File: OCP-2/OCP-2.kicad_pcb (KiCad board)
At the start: 2 copper layers, 90 x 100 mm, 176 parts, among them X1 ico*отверстие*М3, X2 ico*отверстие*М3, X3 ico*отверстие*М3, X4 ico*отверстие*М3

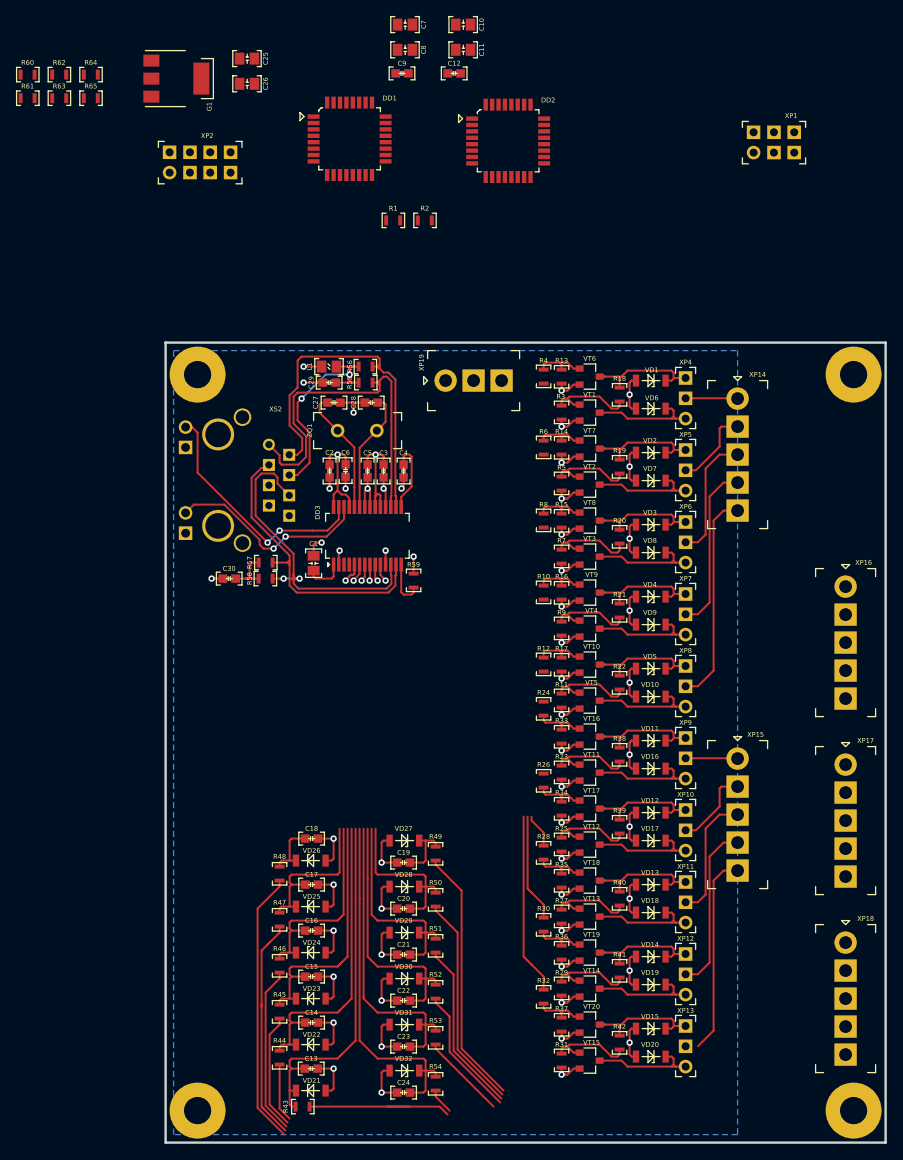
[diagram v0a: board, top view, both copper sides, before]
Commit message: перенесены клеммники, +LDO, +прог.разъем, +МК расположение
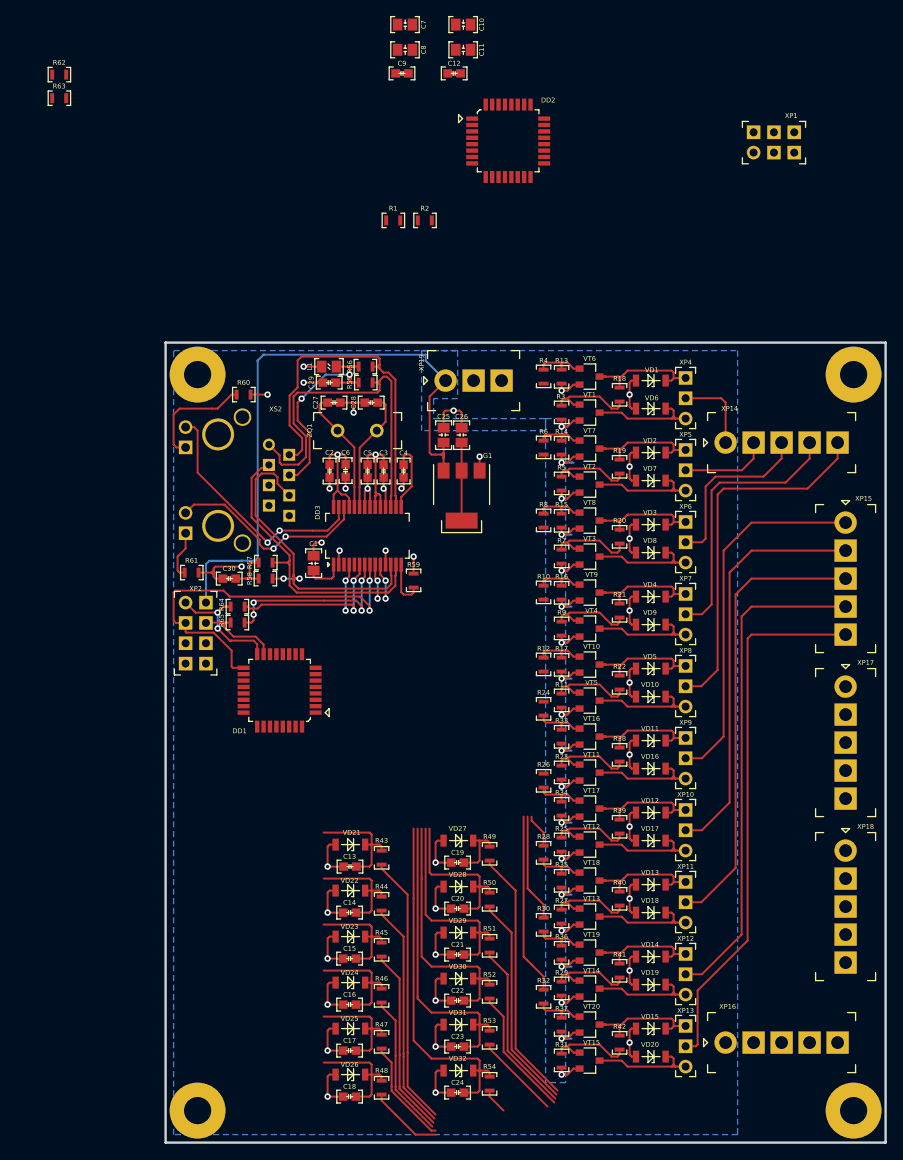
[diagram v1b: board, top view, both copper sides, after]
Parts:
- moved DD1 74.5 mm to (68.5, 96.2), turned to 180 degrees
- moved R64 69.0 mm to (59.0, 83.0), turned to 180 degrees
- moved R65 68.1 mm to (59.0, 85.0), turned to 180 degrees
- moved G1 63.2 mm to (87.0, 69.2), turned to 270 degrees
- moved R61 62.7 mm to (53.2, 78.8)
- moved XP16 58.9 mm to (120.0, 137.5), turned to 0 degrees
- moved C25 54.4 mm to (84.8, 62.5), turned to 90 degrees
- moved XP2 53.8 mm to (52.5, 82.5), turned to 270 degrees
- moved C26 52.7 mm to (87.0, 62.5), turned to 90 degrees
- moved R60 48.3 mm to (59.8, 56.5)
- moved R43 32.7 mm to (77.0, 114.4), turned to 270 degrees
- moved C18 32.6 mm to (73.0, 144.2), turned to 0 degrees
- moved XP15 32.4 mm to (135.0, 72.5)
- moved VD21 30.8 mm to (71.2, 112.8), turned to 0 degrees
- moved R48 29.6 mm to (77.0, 143.1)
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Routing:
- net 5V: track 39.4 -> 117.4 mm
- net /ETH.CLK: track 2.02 -> 48.3 mm, vias 1 -> 2
- net /DOUT10: track 25.0 -> 67.4 mm
- net /DOUT7: track 10.1 -> 51.3 mm
- net /DOUT9: track 21.1 -> 62.3 mm
- net /DOUT8: track 15.9 -> 56.8 mm
- net /DOUT6: track 6.46 -> 45.8 mm
- net /MC.DIN1: track 44.8 -> 14.5 mm
- net GND: track 180.4 -> 209.1 mm, vias 44 -> 47
- net /DIN6: track 34.3 -> 9.26 mm
- net /MC.DIN2: track 38.1 -> 14.5 mm
- net Net-(DD3-Pad7): track 2.17 -> 23.8 mm, vias 1 -> 4
- net /DIN2: track 7.27 -> 28.7 mm
- net /DOUT5: track 26.6 -> 45.6 mm
- net Net-(DD3-Pad6): track 2.31 -> 20.6 mm, vias 1 -> 2
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- added copper zone on B.Cu, net 5V

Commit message: завершенеа трассировка
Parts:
- removed C11, C8: Конденсатор*10мкФ*16В*0805, N_RLC:Конденсатор_SMD_IEC_0805
- added C31: Конденсатор*10мкФ*16В*0805, N_RLC:Конденсатор_SMD_IEC_0805, F.Cu at (85.5, 76.0)
- added X5: ico*LOGO_NIKITOS_10х10, N_ICO:ni_10x10, F.Cu at (72.8, 115.0)
- moved C10 99.5 mm to (83.2, 109.8), turned to 270 degrees
- moved R62 89.3 mm to (54.8, 104.0)
- moved R63 84.5 mm to (54.8, 102.0)
- moved DD2 83.2 mm to (80.0, 104.8), turned to 90 degrees
- moved C7 82.9 mm to (73.8, 93.0)
- moved C9 77.0 mm to (58.5, 90.5), turned to 90 degrees
- moved C12 75.9 mm to (84.8, 92.2), turned to 90 degrees
- moved XP1 72.0 mm to (90.0, 90.0), turned to 270 degrees
- moved R1 64.2 mm to (56.8, 95.1), turned to 270 degrees
- moved R2 57.7 mm to (86.8, 92.2), turned to 90 degrees
- moved C19 38.0 mm to (60.2, 142.5)
- moved R49 38.0 mm to (64.2, 141.4)
- moved VD27 38.0 mm to (58.5, 139.8)
- moved C24 23.5 mm to (72.0, 125.2)
- moved R54 23.5 mm to (76.0, 124.1)
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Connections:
- C13 pad 2: /MC.DIN1 -> /MC.DIN7
- C14 pad 2: /MC.DIN2 -> /MC.DIN6
- C15 pad 2: /MC.DIN3 -> /MC.DIN5
- C16 pad 2: /MC.DIN4 -> /MC.DIN1
- C17 pad 2: /MC.DIN5 -> /MC.DIN2
- C18 pad 2: /MC.DIN6 -> /MC.DIN3
- C19 pad 2: /MC.DIN7 -> /MC.DIN4
- C20 pad 2: /MC.DIN8 -> /MC.DIN12
- C21 pad 2: /MC.DIN9 -> /MC.DIN11
- C23 pad 2: /MC.DIN11 -> /MC.DIN9
- C24 pad 2: /MC.DIN12 -> /MC.DIN8
- DD1 pad 1: /MC.DIN1 -> /MC.DIN7
- DD1 pad 10: /MC.DIN4 -> /MC.OUT3
- DD1 pad 11: /MC.DIN5 -> /MC.OUT2
- DD1 pad 12: /MC.DIN6 -> /MC.OUT1
- DD1 pad 19: Net-(DD1-Pad19) -> /MC.DIN4
- DD1 pad 2: /MC.DIN2 -> /MC.DIN8
- DD1 pad 22: Net-(DD1-Pad22) -> /MC.DIN3
- DD1 pad 23: /MC.OUT1 -> /MC.DIN2
- DD1 pad 24: /MC.OUT2 -> /MC.DIN1
- DD1 pad 25: /MC.OUT3 -> /MC.DIN5
- DD1 pad 26: /MC.OUT4 -> /MC.DIN6
- DD1 pad 7: Net-(DD1-Pad7) -> /MC.OUT6
- DD1 pad 8: Net-(DD1-Pad8) -> /MC.OUT5
- DD1 pad 9: /MC.DIN3 -> /MC.OUT4
- DD2 pad 1: Net-(DD2-Pad1) -> /MC.DIN12
- DD2 pad 10: /MC.DIN8 -> Net-(DD2-Pad10)
- DD2 pad 11: /MC.DIN9 -> /MC.OUT10
- DD2 pad 12: /MC.DIN10 -> /MC.OUT9
- DD2 pad 13: /MC.DIN11 -> /MC.OUT8
- DD2 pad 14: /MC.DIN12 -> /MC.OUT7
- DD2 pad 23: /MC.OUT5 -> Net-(DD2-Pad23)
- DD2 pad 24: /MC.OUT6 -> Net-(DD2-Pad24)
- DD2 pad 25: /MC.OUT7 -> Net-(DD2-Pad25)
- DD2 pad 26: /MC.OUT8 -> Net-(DD2-Pad26)
- DD2 pad 30: /MC.OUT9 -> /MC.DIN9
- DD2 pad 31: /MC.OUT10 -> /MC.DIN10
- DD2 pad 32: Net-(DD2-Pad32) -> /MC.DIN11
- DD2 pad 9: /MC.DIN7 -> Net-(DD2-Pad9)
- R43 pad 1: /MC.DIN1 -> /MC.DIN7
- R43 pad 2: /DIN1 -> /DIN7
- R44 pad 1: /MC.DIN2 -> /MC.DIN6
- R44 pad 2: /DIN2 -> /DIN6
- R45 pad 1: /MC.DIN3 -> /MC.DIN5
- R45 pad 2: /DIN3 -> /DIN5
- R46 pad 1: /MC.DIN4 -> /MC.DIN1
- R46 pad 2: /DIN4 -> /DIN1
- R47 pad 1: /MC.DIN5 -> /MC.DIN2
- R47 pad 2: /DIN5 -> /DIN2
- R48 pad 1: /MC.DIN6 -> /MC.DIN3
- R48 pad 2: /DIN6 -> /DIN3
- R49 pad 1: /MC.DIN7 -> /MC.DIN4
- R49 pad 2: /DIN7 -> /DIN4
- R50 pad 1: /MC.DIN8 -> /MC.DIN12
- R50 pad 2: /DIN8 -> /DIN12
- R51 pad 1: /MC.DIN9 -> /MC.DIN11
- R51 pad 2: /DIN9 -> /DIN11
- R53 pad 1: /MC.DIN11 -> /MC.DIN9
- R53 pad 2: /DIN11 -> /DIN9
- R54 pad 1: /MC.DIN12 -> /MC.DIN8
- R54 pad 2: /DIN12 -> /DIN8
- VD21 pad 2: /MC.DIN1 -> /MC.DIN7
- VD22 pad 2: /MC.DIN2 -> /MC.DIN6
- VD23 pad 2: /MC.DIN3 -> /MC.DIN5
- VD24 pad 2: /MC.DIN4 -> /MC.DIN1
- VD25 pad 2: /MC.DIN5 -> /MC.DIN2
- VD26 pad 2: /MC.DIN6 -> /MC.DIN3
- VD27 pad 2: /MC.DIN7 -> /MC.DIN4
- VD28 pad 2: /MC.DIN8 -> /MC.DIN12
- VD29 pad 2: /MC.DIN9 -> /MC.DIN11
- VD31 pad 2: /MC.DIN11 -> /MC.DIN9
- VD32 pad 2: /MC.DIN12 -> /MC.DIN8
- XP16 pad 1: /DIN1 -> /DIN4
- XP16 pad 2: /DIN2 -> /DIN3
- XP16 pad 3: /DIN3 -> /DIN2
- XP16 pad 4: /DIN4 -> /DIN1
- XP17 pad 1: /DIN5 -> /DIN12
- XP17 pad 2: /DIN6 -> /DIN11
- XP17 pad 3: /DIN7 -> /DIN10
- XP17 pad 4: /DIN8 -> /DIN9
- XP18 pad 1: /DIN9 -> /DIN8
- XP18 pad 2: /DIN10 -> /DIN7
- XP18 pad 3: /DIN11 -> /DIN6
- XP18 pad 4: /DIN12 -> /DIN5
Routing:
- net 3V3: track 49.7 -> 232.3 mm, vias 3 -> 11
- net /DIN12: track 3.22 -> 99.5 mm
- net /DIN11: track 10.8 -> 92.0 mm
- net /DIN6: track 9.26 -> 82.4 mm
- net /DIN8: track 27.0 -> 97.3 mm
- net /DIN10: track 16.4 -> 84.4 mm
- net /DIN4: track 18.1 -> 80.7 mm
- net /DIN5: track 13.4 -> 75.8 mm
- net /MC.OUT1: track 0.00 -> 61.4 mm
- net /DIN3: track 23.4 -> 81.6 mm
- net GND: track 209.1 -> 267.2 mm, vias 47 -> 70
- net /DIN7: track 32.3 -> 89.1 mm
- net /DIN2: track 28.7 -> 83.2 mm
- net /DIN9: track 21.7 -> 76.1 mm
- net /MC.OUT2: track 0.00 -> 53.4 mm
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- added copper zone on B.Cu, net 3V3
- added copper zone on F.Cu, net GND
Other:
- board text added: "1+"
- board text added: "1-"
- board text added: "10+"
- board text added: "10-"
- board text added: "10C"
- board text added: "1C"
- board text added: "2+"
- board text added: "2-"
- board text added: "2C"
- board text added: "3+"
- board text added: "3-"
- board text added: "3C"
- board text added: "4+"
- board text added: "4-"
- board text added: "4C"
- board text added: "5+"
- board text added: "5-"
- board text added: "5C"
- board text added: "5V"
- board text added: "6+"
- board text added: "6-"
- board text added: "6C"
- board text added: "7+"
- board text added: "7-"
- board text added: "7C"
- board text added: "8+"
- board text added: "8-"
- board text added: "8C"
- board text added: "9+"
- board text added: "9-"
- board text added: "9C"
- board text added: "GND"
- board text added: "M.IN1"
- board text added: "M.IN2"
- board text added: "M.IN3"
- board text added: "M.IN4"
- board text added: "M.IN5"
- board text added: "M.IN6"
- board text added: "M.IN7"
- board text added: "M.IN8"
- board text added: "M.IN9"
- board text added: "M.OUT1"
- board text added: "M.OUT2"
- board text added: "M.OUT3"
- board text added: "M.OUT4"
- board text added: "M.OUT5"
- board text added: "M.OUT6"
- board text added: "MASTER"
- board text added: "MI"
- board text added: "MO"
- board text added: "N.C."
- board text added: "RES"
- board text added: "RX"
- board text added: "S.IN10"
- board text added: "S.IN11"
- board text added: "S.IN12"
- board text added: "S.OUT10"
- board text added: "S.OUT7"
- board text added: "S.OUT8"
- board text added: "S.OUT9"
- board text added: "SCK"
- board text added: "SLAVE"
- board text added: "TX"

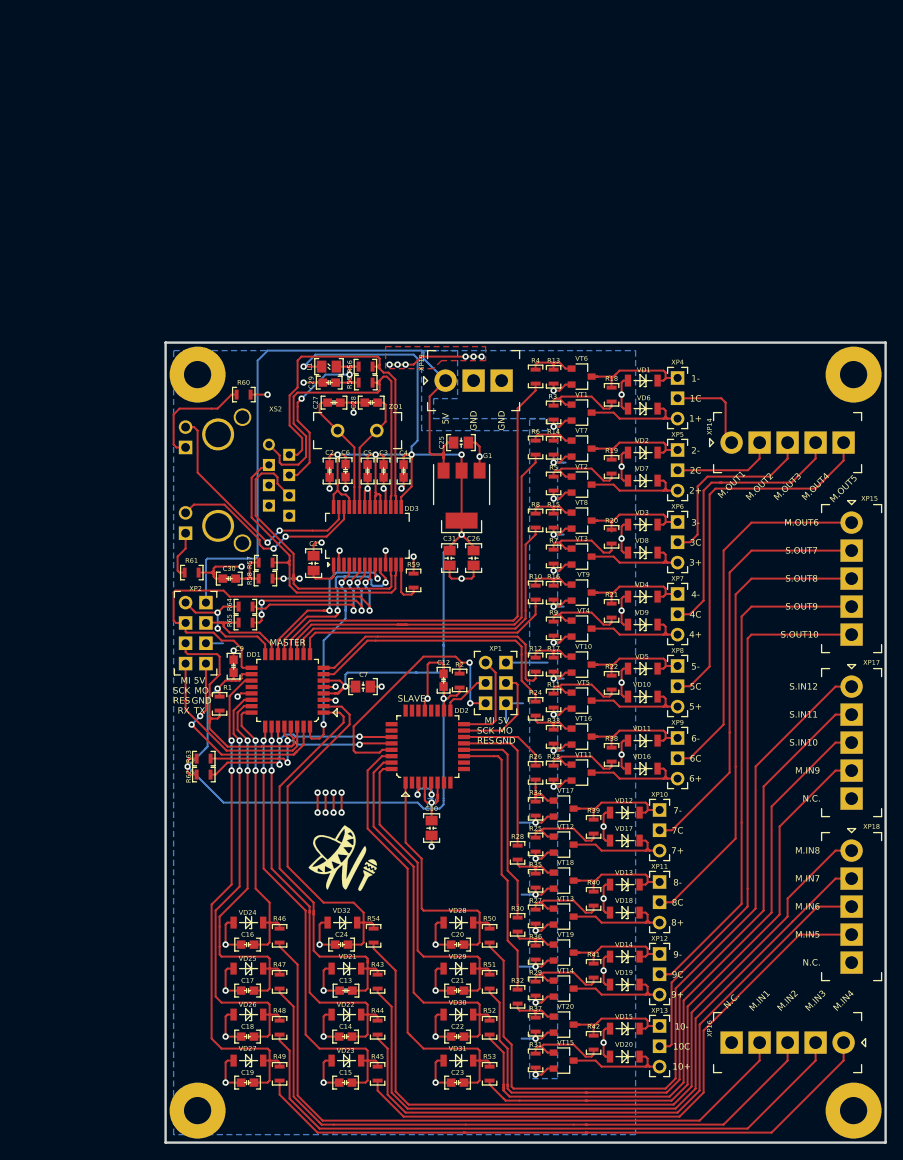
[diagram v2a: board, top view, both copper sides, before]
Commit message: добавлена поясняющая маркировка
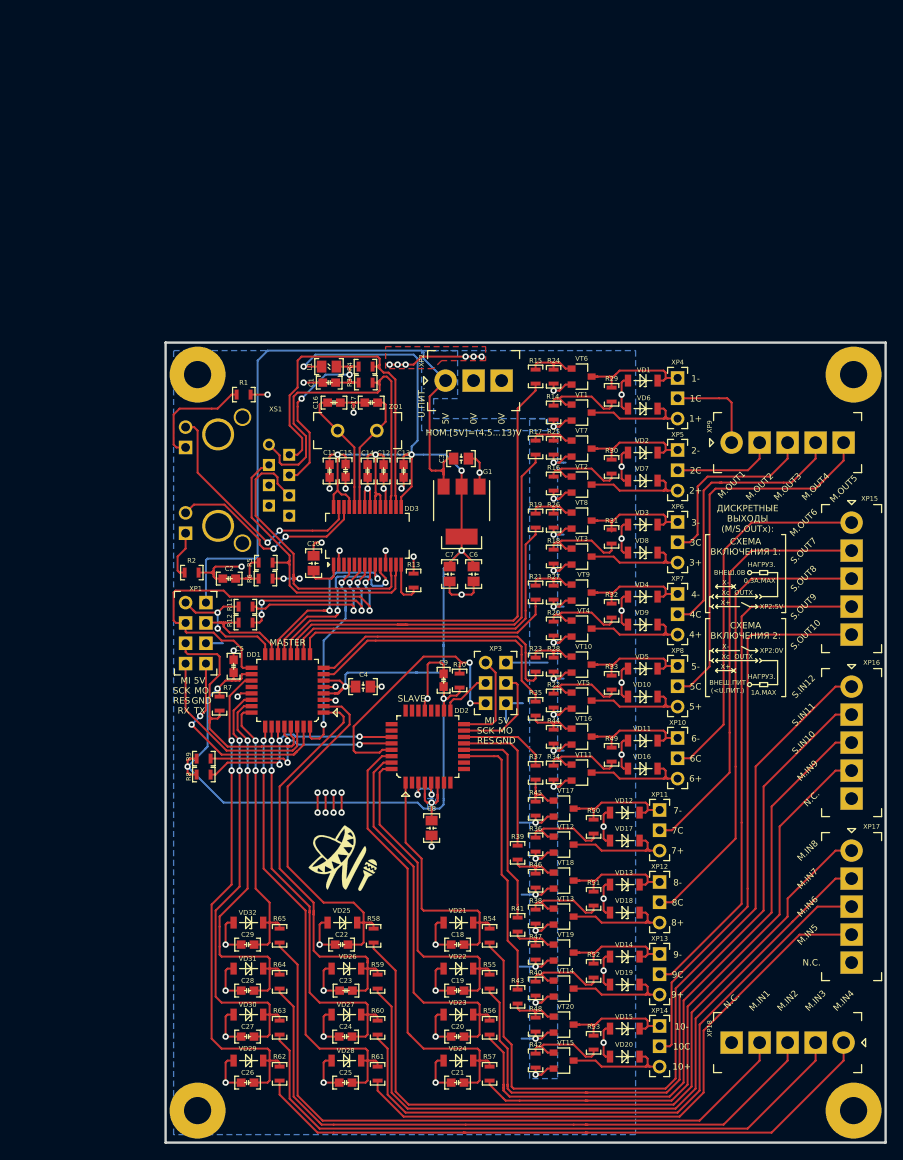
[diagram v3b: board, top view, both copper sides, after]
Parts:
- moved C3 2.00 mm to (86.0, 64.5)
- moved C6 2.00 mm to (88.5, 78.0)
- moved C7 2.00 mm to (85.5, 78.0)
- moved G1 2.00 mm to (87.0, 71.2)
- renumbered C29 to C1, C1 to C10, C2 to C11, C3 to C12, C4 to C13, C5 to C14, C6 to C15, C27 to C16, C28 to C17, C20 to C18, C21 to C19, C30 to C2, C22 to C20, C23 to C21, C24 to C22, C13 to C23, C14 to C24, C15 to C25, C19 to C26, C18 to C27, C17 to C28, C16 to C29, C25 to C3, C7 to C4, C9 to C5, C26 to C6, C31 to C7, C10 to C8, C12 to C9, R60 to R1, R2 to R10, R64 to R11, R65 to R12, R59 to R13, R3 to R14, R4 to R15, R5 to R16, R6 to R17, R7 to R18, R8 to R19, R61 to R2, R9 to R20, R10 to R21, R11 to R22, R12 to R23, R13 to R24, R14 to R25, R15 to R26, R16 to R27, R17 to R28, R18 to R29, R55 to R3, R19 to R30, R20 to R31, R21 to R32, R22 to R33, R23 to R34, R24 to R35, R25 to R36, R26 to R37, R27 to R38, R28 to R39, R56 to R4, R29 to R40, R30 to R41, R31 to R42, R32 to R43, R33 to R44, R34 to R45, R35 to R46, R36 to R47, R37 to R48, R38 to R49, R57 to R5, R39 to R50, R40 to R51, R41 to R52, R42 to R53, R50 to R54, R51 to R55, R52 to R56, R53 to R57, R54 to R58, R43 to R59, R58 to R6, R44 to R60, R45 to R61, R49 to R62, R48 to R63, R47 to R64, R46 to R65, R1 to R7, R62 to R8, R63 to R9, VD28 to VD21, VD29 to VD22, VD30 to VD23, VD31 to VD24, VD32 to VD25, VD21 to VD26, VD22 to VD27, VD23 to VD28, VD27 to VD29, VD26 to VD30, VD25 to VD31, VD24 to VD32, XP2 to XP1, XP9 to XP10, XP10 to XP11, XP11 to XP12, XP12 to XP13, XP13 to XP14, XP17 to XP16, XP18 to XP17, XP16 to XP18, XP19 to XP2, XP1 to XP3, XP14 to XP9, XS2 to XS1
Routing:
- net 5V: track 124.1 -> 126.1 mm
- net 3V3: track 232.3 -> 231.1 mm
- net /DOUT1: track 11.2 -> 12.0 mm
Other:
- board text added: "(<U.ПИТ.)"
- board text added: "0,3A.MAX"
- board text added: "0V"
- board text added: "1A.MAX"
- board text added: "OUTX"
- board text added: "U.ПИТ."
- board text added: "X+"
- board text added: "X-"
- board text added: "XP2:0V"
- board text added: "XP2:5V"
- board text added: "Xc"
- board text added: "ВНЕШ.0В"
- board text added: "ВНЕШ.ПИТ"
- board text added: "ДИСКРЕТНЫЕ ВЫХОДЫ (M/S.OUTx):"
- board text added: "НАГРУЗ."
- board text added: "НОМ.[5V]=(4.5...13)V"
- board text added: "СХЕМА ВКЛЮЧЕНИЯ 1:"
- board text added: "СХЕМА ВКЛЮЧЕНИЯ 2:"
